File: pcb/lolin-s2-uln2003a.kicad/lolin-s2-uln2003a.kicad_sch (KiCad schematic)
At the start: 18 parts, among them J1 Conn_S2_Left, J10 Micro_SD_TF_PUSH, J11 Vin Barrel-Jack, J12 Conn_LED2, J2 Conn_S2_Right, J3 Conn_PWR, J4 Conn_Motor, J5 Conn_LED1, J6 Conn_LED3, J7 Conn_I2S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

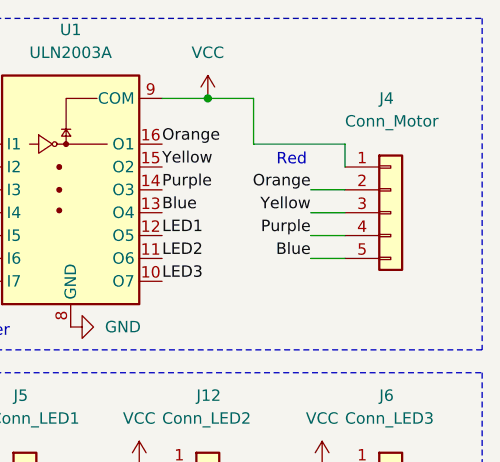
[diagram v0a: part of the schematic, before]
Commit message: fixed rotation of motor-connector
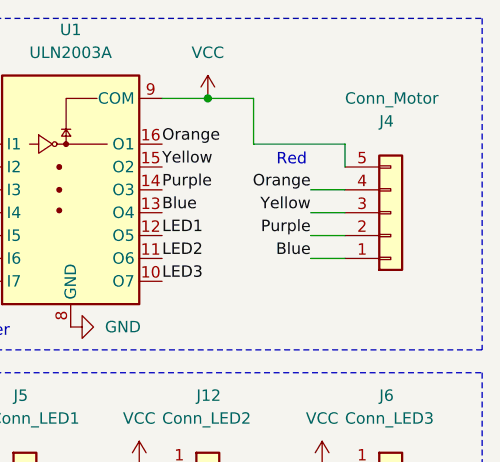
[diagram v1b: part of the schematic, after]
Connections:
- net Blue: now also J4.1 (Pin_1); no longer J4.5 (Pin_5)
- net Orange: now also J4.4 (Pin_4); no longer J4.2 (Pin_2)
- net Purple: now also J4.2 (Pin_2); no longer J4.4 (Pin_4)
- net VCC: now also J4.5 (Pin_5); no longer J4.1 (Pin_1)
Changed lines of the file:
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@@
   (title_block
     (title "Lolin-S2-uln2003a Support PCB")
-    (date "2025-05-20")
-    (rev "1.00")
+    (date "2025-08-25")
+    (rev "1.01")
     (company "Bernhard Bablok")
     (comment 1 "https://github.com/bablokb/motor-turntable")
@@
     )
   )
-  (symbol (lib_id "Connector_Generic:Conn_01x05") (at 251.46 58.42 0) (unit 1)
+  (symbol (lib_id "Connector_Generic:Conn_01x05") (at 251.46 58.42 0) (mirror x) (unit 1)
     (in_bom no) (on_board yes) (dnp no)
-    (property "Reference" "J4" (at 250.19 45.72 0)
-      (effects (font (size 1.27 1.27)) (justify left))
-    )
-    (property "Value" "Conn_Motor" (at 246.38 48.26 0)
-      (effects (font (size 1.27 1.27)) (justify left))
-    )
+    (property "Reference" "J4" (at 250.19 48.26 0)
+      (effects (font (size 1.27 1.27)) (justify left))
+    )
+    (property "Value" "Conn_Motor" (at 246.38 45.72 0)
+      (effects (font (size 1.27 1.27)) (justify left))
+    )

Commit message: Rev. 2.00 of support-pcb
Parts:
- removed J10: Micro_SD_TF_PUSH, user:TF-Push, symbol user:Micro_SD_TF_PUSH
- removed J11: Vin Barrel-Jack, user:BarrelJack_CUI_PJ-102AH_Horizontal, symbol Connector:Barrel_Jack_Switch
- removed J7: Conn_I2S, user:MAX98357A_Breakout, symbol user:MAX98357A_Breakout
- removed JP1: JMP_GAIN, Connector_PinHeader_2.54mm:PinHeader_1x03_P2.54mm_Vertical, symbol Jumper:Jumper_3_Open
- added C1: 100nF, Capacitor_SMD:C_0402_1005Metric, symbol Device:C_Small
- added J10: Conn_Spk, Connector_JST:JST_XH_B2B-XH-A_1x02_P2.50mm_Vertical, symbol Connector_Generic:Conn_01x02
- added J11: Conn_SUR1, Connector_JST:JST_SUR_BM02B-SURS-TF_1x02-1MP_P0.80mm_Vertical, symbol Connector_Generic:Conn_01x02
- added J13: Conn_SUR2, Connector_JST:JST_SUR_BM02B-SURS-TF_1x02-1MP_P0.80mm_Vertical, symbol Connector_Generic:Conn_01x02
- added J14: Conn_SUR3, Connector_JST:JST_SUR_BM02B-SURS-TF_1x02-1MP_P0.80mm_Vertical, symbol Connector_Generic:Conn_01x02
- added J15: Conn_Neo, Connector_JST:JST_XH_B3B-XH-A_1x03_P2.50mm_Vertical, symbol Connector_Generic:Conn_01x03
- added J16: Conn_Extra, Connector_PinHeader_2.54mm:PinHeader_2x05_P2.54mm_Vertical, symbol Connector_Generic:Conn_02x05_Odd_Even
- added J7: Conn_Player, Connector_JST:JST_XH_B2B-XH-A_1x02_P2.50mm_Vertical, symbol Connector_Generic:Conn_01x02
- added R1: 33, Resistor_SMD:R_0402_1005Metric, symbol Device:R_Small
- added U2: DFR0299, user:DFR0299, symbol user:DFR0299
- added U3: 74LVC1G17, user:74LVC1G17GW_125, symbol user:74LVC1G17GW_125
- J3: footprint Connector_PinHeader_2.54mm:PinHeader_1x04_P2.54mm_Vertical -> Connector_PinHeader_2.54mm:PinHeader_1x05_P2.54mm_Vertical; symbol Connector_Generic:Conn_01x04 -> Connector_Generic:Conn_01x05
- J8: footprint Connector_PinHeader_2.54mm:PinHeader_1x07_P2.54mm_Vertical -> Connector_PinHeader_2.54mm:PinHeader_1x06_P2.54mm_Vertical; symbol Connector_Generic:Conn_01x07 -> Connector_Generic:Conn_01x06
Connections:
- net +3V3: now also J16.1 (Pin_1), J16.2 (Pin_2); no longer J8.7 (Pin_7)
- net GND: now also J3.2 (Pin_2), J3.5 (Pin_5), C1.1, J15.3 (Pin_3), J16.3 (Pin_3), J16.4 (Pin_4), U2.10 (GND), U2.7 (GND), U3.3 (GND); no longer J3.1 (Pin_1), J3.4 (Pin_4)
- net GPIO11: now also U2.2 (RX)
- net GPIO12: now also U2.3 (TX)
- net GPIO38: now also J16.8 (Pin_8)
- net GPIO4: now also J16.5 (Pin_5)
- net GPIO6: now also J16.7 (Pin_7)
- net GPIO8: now also J16.9 (Pin_9)
- net GPIO9: now also U3.2 (A)
- net LED1: now also J11.2 (Pin_2)
- net LED2: now also J13.2 (Pin_2)
- net LED3: now also J14.2 (Pin_2)
- net VBUS: now also J3.1 (Pin_1), J3.3 (Pin_3), C1.2, J15.1 (Pin_1), U2.1 (VCC), U3.5 (VCC); no longer J3.2 (Pin_2)
- net VCC: now also J3.4 (Pin_4), J11.1 (Pin_1), J13.1 (Pin_1), J14.1 (Pin_1); no longer J3.3 (Pin_3)
- net GPIO40: now reaches J2.1 (Pin_1)
- net GPIO40: now also J16.10 (Pin_10)
- net GPIO36: now reaches J2.5 (Pin_5)
- net GPIO36: now also J16.6 (Pin_6)
- net GPIO10: no longer names the net of J1.12 (Pin_12)
- new net: J15.2 (Pin_2), R1.2
- new net: R1.1, U3.4 (Y)
- new net: J7.2 (Pin_2), U2.11 (IO2)
- new net: J10.1 (Pin_1), U2.6 (SPK1)
- new net: J10.2 (Pin_2), U2.8 (SPK2)
- new net: J7.1 (Pin_1), U2.9 (IO1)
- no-connect marks 9 -> 12
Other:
- note added: "DFPlayer-Mini"
- note added: "Extra GPIOs (optional)"
- note added: "GPIO10"
- note added: "Neopixel (optional)"
- note removed: "Barrel-Jack optional (connect VBUS-VCC)"
- note removed: "GPIO36"
- note removed: "GPIO40"
- note removed: "I2S"
- note removed: "MicroSD-Card-Reader"
- note removed: "VBUS: 6dB n.c.: 9dB GND: 12dB"
- moved on the sheet: J1, J12, J2, J4, J5, J6, J9, U1
